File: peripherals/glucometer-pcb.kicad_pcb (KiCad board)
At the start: 2 copper layers, 244.2 x 145.5 mm, 126 parts, among them U1 ESP32_DevKit_V1_DOIT

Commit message: added 3D models
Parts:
- removed the 100nF1 at (35.7, 153.9)
- removed the 100nF1 at (72.2, 30.6)
- removed the 100nF1 at (170.3, 156.4)
- removed the 100nF1 at (234.8, 30.6)
- removed the 100nF1 at (181.4, 30.6)
- removed the 100nF1 at (123.0, 30.6)
- removed the 3V3_OUT1 at (88.9, 21.8)
- removed the 3V3_OUT1 at (198.1, 21.8)
- removed the 3V3_OUT1 at (161.5, 139.7)
- removed the 3V3_OUT1 at (251.5, 21.8)
- removed the 3V3_OUT1 at (139.7, 21.8)
- removed the 3V3_OUT1 at (26.9, 137.1)
- removed the BATTERY1 at (26.9, 151.3)
- removed the BATTERY1 at (237.3, 21.8)
- removed the BATTERY1 at (183.9, 21.8)
- removed the BATTERY1 at (125.5, 21.8)
- removed the BATTERY1 at (74.7, 21.8)
- removed the BATTERY1 at (161.5, 153.9)
- removed the BZ1 at (148.7, 32.9)
- removed the BZ1 at (172.6, 130.7)
- removed the BZ1 at (207.1, 32.9)
- removed the BZ1 at (260.5, 32.9)
- removed the BZ1 at (97.9, 32.9)
- removed the BZ1 at (38.0, 128.2)
- removed the D1 at (253.2, 145.1)
- removed the D1 at (83.5, 113.5)
- removed the D1 at (192.7, 113.5)
- removed the D1 at (246.1, 113.5)
- removed the D1 at (118.5, 142.5)
- removed the D1 at (134.3, 113.5)
- removed the GND1 at (238.1, 42.0)
- removed the GND1 at (126.4, 42.0)
- removed the GND1 at (47.1, 150.5)
- removed the GND1 at (75.6, 42.0)
- removed the GND1 at (181.7, 153.0)
- removed the GND1 at (184.8, 42.0)
- removed the INTERRUPT_GPIO1 at (161.5, 130.0)
- removed the INTERRUPT_GPIO1 at (149.4, 21.8)
- removed the INTERRUPT_GPIO1 at (98.6, 21.8)
- removed the INTERRUPT_GPIO1 at (261.2, 21.8)
- removed the INTERRUPT_GPIO1 at (26.9, 127.4)
- removed the INTERRUPT_GPIO1 at (207.8, 21.8)
- removed the R1 at (82.6, 35.7)
- removed the R1 at (133.4, 35.7)
- removed the R1 at (175.4, 146.0)
- removed the R1 at (191.8, 35.7)
- removed the R1 at (40.8, 143.5)
- removed the R1 at (245.1, 35.7)
- removed the R2 at (77.8, 35.7)
- removed the R2 at (187.1, 35.7)
- removed the R2 at (40.8, 148.2)
- removed the R2 at (128.6, 35.7)
- removed the R2 at (240.4, 35.7)
- removed the R2 at (175.4, 150.8)
- removed the REF** at (22.8, 154.8)
- removed the REF** at (71.3, 114.5)
- removed the REF** at (157.4, 157.3)
- removed the REF** at (261.6, 17.7)
- removed the REF** at (254.2, 157.3)
- removed the REF** at (122.1, 17.7)
- removed the REF** at (122.1, 114.5)
- removed the REF** at (207.8, 114.5)
- removed the REF** at (149.4, 114.5)
- removed the REF** at (149.8, 17.7)
- removed the REF** at (233.8, 17.7)
- removed the REF** at (261.2, 114.5)
- removed the REF** at (254.2, 130.0)
- removed the REF** at (98.6, 114.5)
- removed the REF** at (157.4, 129.6)
- removed the REF** at (119.6, 154.8)
- removed the REF** at (180.5, 17.7)
- removed the REF** at (99.0, 17.7)
- removed the REF** at (71.3, 17.7)
- removed the REF** at (180.5, 114.5)
- removed the REF** at (119.6, 127.5)
- removed the REF** at (22.8, 127.1)
- removed the REF** at (233.8, 114.5)
- removed the REF** at (208.2, 17.7)
- removed the SCL1 at (92.4, 42.0)
- removed the SCL1 at (47.1, 133.7)
- removed the SCL1 at (201.6, 42.0)
- removed the SCL1 at (181.7, 136.2)
- removed the SCL1 at (254.9, 42.0)
- removed the SCL1 at (143.2, 42.0)
- removed the SDA1 at (196.0, 42.0)
- removed the SDA1 at (137.6, 42.0)
- removed the SDA1 at (86.8, 42.0)
- removed the SDA1 at (47.1, 139.3)
- removed the SDA1 at (249.3, 42.0)
- removed the SDA1 at (181.7, 141.8)
- removed the SIGNAL_IN1 at (81.1, 21.8)
- removed the SIGNAL_IN1 at (161.5, 147.5)
- removed the SIGNAL_IN1 at (26.9, 144.9)
- removed the SIGNAL_IN1 at (131.9, 21.8)
- removed the SIGNAL_IN1 at (190.3, 21.8)
- removed the SIGNAL_IN1 at (243.7, 21.8)
- removed the U1 at (246.6, 86.0)
- removed the U1 at (134.8, 86.0)
- removed the U1 at (91.0, 142.1)
- removed the U1 at (193.2, 86.0)
- removed the U1 at (225.7, 144.6)
- removed the U1 at (84.0, 86.0)
- removed the VCC1 at (243.8, 42.0)
- removed the VCC1 at (190.5, 42.0)
- removed the VCC1 at (181.7, 147.3)
- removed the VCC1 at (81.3, 42.0)
- removed the VCC1 at (47.1, 144.8)
- removed the VCC1 at (132.1, 42.0)
- moved U1 0.06 mm to (36.0, 85.9)
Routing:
- net Net-(D1-Pad1): track 560.9 -> 80.1 mm
- net Net-(INTERRUPT_GPIO1-Pad1): track 376.7 -> 53.8 mm
- net Net-(3V3_OUT1-Pad1): track 342.0 -> 48.9 mm
- net Net-(SDA1-Pad1): track 318.6 -> 45.5 mm
- net Net-(100nF1-Pad2): track 313.1 -> 44.7 mm
- net Net-(BZ1-Pad1): track 270.9 -> 38.7 mm
- net Net-(SCL1-Pad1): track 249.0 -> 35.6 mm
- net Net-(BATTERY1-Pad1): track 232.0 -> 33.1 mm
- net Net-(D1-Pad2): track 223.4 -> 31.9 mm
- net Net-(100nF1-Pad1): track 88.0 -> 12.6 mm
- net Net-(BZ1-Pad2): track 55.2 -> 7.89 mm
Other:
- board size 244.2 x 145.5 mm -> 33.3 x 102.6 mm

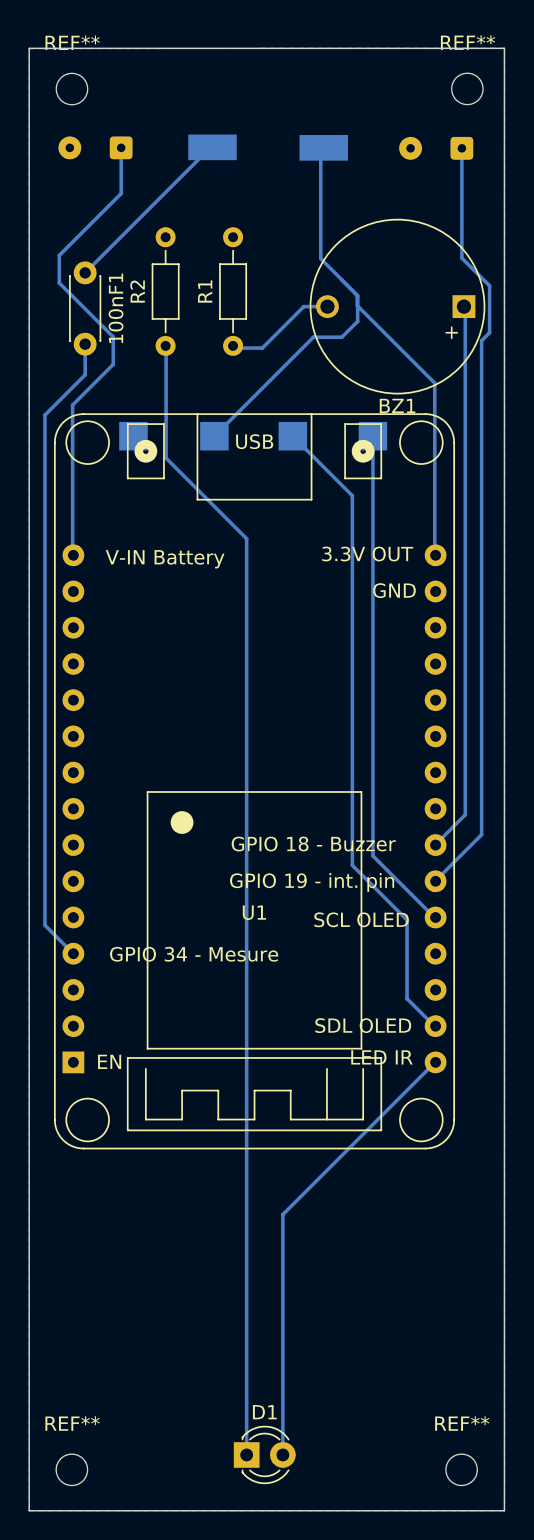
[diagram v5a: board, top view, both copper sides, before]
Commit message: updated pcb pads
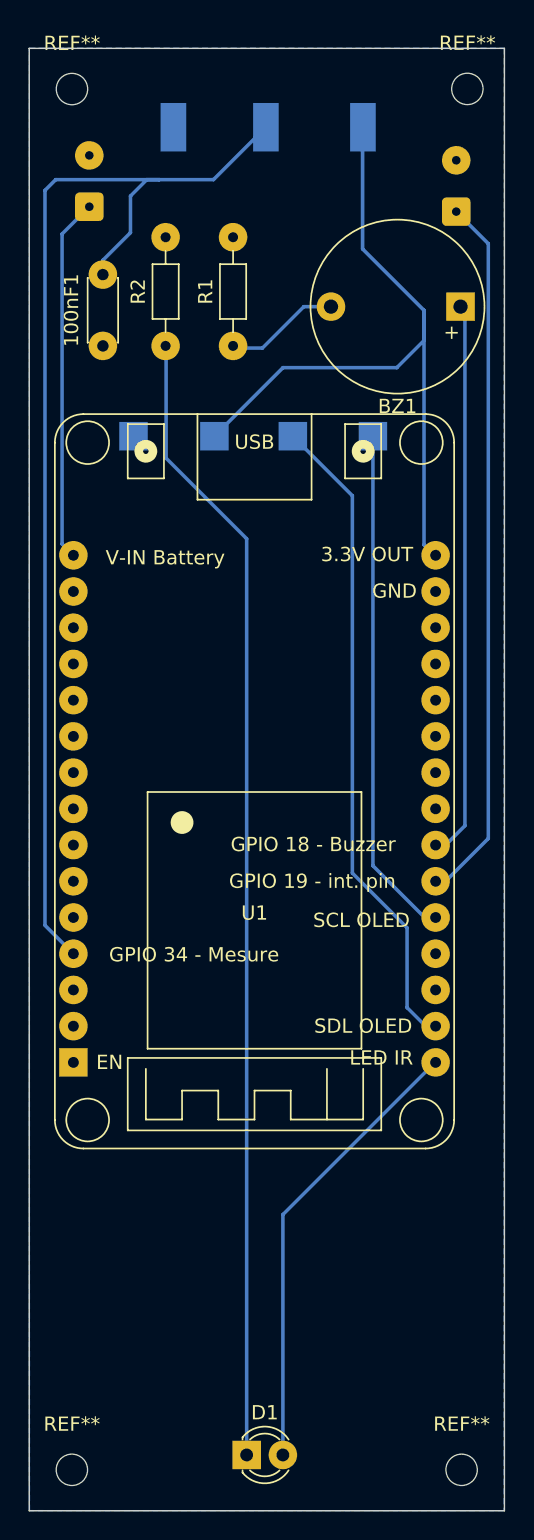
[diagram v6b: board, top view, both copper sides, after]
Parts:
- added GND1: TestPoint, TestPoint:TestPoint_Keystone_5015_Micro-Minature, B.Cu at (30.3, 20.4)
- moved 100nF1 5.27 mm to (25.4, 35.7), turned to 90 degrees
- moved BATTERY1 4.69 mm to (24.4, 25.9), turned to 90 degrees
- moved INTERRUPT_GPIO1 4.46 mm to (50.2, 26.3), turned to 90 degrees
- moved SIGNAL_IN1 4.00 mm to (36.8, 20.4), turned to -90 degrees
- moved 3V3_OUT1 3.11 mm to (43.6, 20.4), turned to -90 degrees
- renumbered GND1 to GND2
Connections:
- 100nF1 pad 1: Net-(100nF1-Pad1) -> GND
- SIGNAL_IN1 pad 1: Net-(100nF1-Pad1) -> Net-(100nF1-Pad2)
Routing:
- net Net-(100nF1-Pad2): track 44.7 -> 80.5 mm
- net Net-(100nF1-Pad1): track 12.6 -> 0.00 mm
- net Net-(BATTERY1-Pad1): track 33.1 -> 25.6 mm
- net Net-(INTERRUPT_GPIO1-Pad1): track 53.8 -> 49.8 mm
- net Net-(3V3_OUT1-Pad1): track 48.9 -> 51.7 mm
- net Net-(BZ1-Pad1): track 38.7 -> 39.4 mm

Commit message: added pdfs
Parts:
- added 100nF1: CAP, Capacitor_THT:C_Disc_D4.3mm_W1.9mm_P5.00mm, F.Cu at (111.1, 37.0)
- added 100nF1: CAP, Capacitor_THT:C_Disc_D4.3mm_W1.9mm_P5.00mm, F.Cu at (47.1, 167.8)
- added 100nF1: CAP, Capacitor_THT:C_Disc_D4.3mm_W1.9mm_P5.00mm, F.Cu at (181.7, 165.3)
- added 100nF1: CAP, Capacitor_THT:C_Disc_D4.3mm_W1.9mm_P5.00mm, F.Cu at (197.9, 37.0)
- added 100nF1: CAP, Capacitor_THT:C_Disc_D4.3mm_W1.9mm_P5.00mm, F.Cu at (154.5, 36.2)
- added 100nF1: CAP, Capacitor_THT:C_Disc_D4.3mm_W1.9mm_P5.00mm, F.Cu at (246.2, 37.0)
- added 100nF1: CAP, Capacitor_THT:C_Disc_D4.3mm_W1.9mm_P5.00mm, F.Cu at (67.7, 36.2)
- added 3V3_OUT1: TestPoint, TestPoint:TestPoint_Keystone_5015_Micro-Minature, B.Cu at (31.8, 149.6)
- added 3V3_OUT1: TestPoint, TestPoint:TestPoint_Keystone_5015_Micro-Minature, B.Cu at (264.4, 21.6)
- added 3V3_OUT1: TestPoint, TestPoint:TestPoint_Keystone_5015_Micro-Minature, B.Cu at (216.2, 21.6)
- added 3V3_OUT1: TestPoint, TestPoint:TestPoint_Keystone_5015_Micro-Minature, B.Cu at (172.8, 20.9)
- added 3V3_OUT1: TestPoint, TestPoint:TestPoint_Keystone_5015_Micro-Minature, B.Cu at (86.0, 20.9)
- added 3V3_OUT1: TestPoint, TestPoint:TestPoint_Keystone_5015_Micro-Minature, B.Cu at (166.4, 147.1)
- added 3V3_OUT1: TestPoint, TestPoint:TestPoint_Keystone_5015_Micro-Minature, B.Cu at (129.3, 21.6)
- added BATTERY1: Battery_Cell, Connector_Wire:SolderWire-0.1sqmm_1x02_P3.6mm_D0.4mm_OD1mm, B.Cu at (197.0, 27.2)
- added BATTERY1: Battery_Cell, Connector_Wire:SolderWire-0.1sqmm_1x02_P3.6mm_D0.4mm_OD1mm, B.Cu at (110.1, 27.2)
- added BATTERY1: Battery_Cell, Connector_Wire:SolderWire-0.1sqmm_1x02_P3.6mm_D0.4mm_OD1mm, B.Cu at (172.0, 166.3)
- added BATTERY1: Battery_Cell, Connector_Wire:SolderWire-0.1sqmm_1x02_P3.6mm_D0.4mm_OD1mm, B.Cu at (66.8, 26.5)
- added BATTERY1: Battery_Cell, Connector_Wire:SolderWire-0.1sqmm_1x02_P3.6mm_D0.4mm_OD1mm, B.Cu at (153.6, 26.5)
- added BATTERY1: Battery_Cell, Connector_Wire:SolderWire-0.1sqmm_1x02_P3.6mm_D0.4mm_OD1mm, B.Cu at (245.2, 27.2)
- added BATTERY1: Battery_Cell, Connector_Wire:SolderWire-0.1sqmm_1x02_P3.6mm_D0.4mm_OD1mm, B.Cu at (37.4, 168.8)
- added BZ1: Buzzer, Buzzer_Beeper:MagneticBuzzer_ProSignal_ABI-009-RC, F.Cu at (92.2, 33.5)
- added BZ1: Buzzer, Buzzer_Beeper:MagneticBuzzer_ProSignal_ABI-009-RC, F.Cu at (44.4, 143.4)
- added BZ1: Buzzer, Buzzer_Beeper:MagneticBuzzer_ProSignal_ABI-009-RC, F.Cu at (222.4, 34.2)
- added BZ1: Buzzer, Buzzer_Beeper:MagneticBuzzer_ProSignal_ABI-009-RC, F.Cu at (179.0, 33.5)
- added BZ1: Buzzer, Buzzer_Beeper:MagneticBuzzer_ProSignal_ABI-009-RC, F.Cu at (135.6, 34.2)
- added BZ1: Buzzer, Buzzer_Beeper:MagneticBuzzer_ProSignal_ABI-009-RC, F.Cu at (270.6, 34.2)
- added BZ1: Buzzer, Buzzer_Beeper:MagneticBuzzer_ProSignal_ABI-009-RC, F.Cu at (179.0, 140.8)
- added D1: EMITTER, LED_THT:LED_D3.0mm_Clear, F.Cu at (164.6, 114.0)
- added D1: EMITTER, LED_THT:LED_D3.0mm_Clear, F.Cu at (259.5, 155.2)
- added D1: EMITTER, LED_THT:LED_D3.0mm_Clear, F.Cu at (77.8, 114.0)
- added D1: EMITTER, LED_THT:LED_D3.0mm_Clear, F.Cu at (121.2, 114.7)
- added D1: EMITTER, LED_THT:LED_D3.0mm_Clear, F.Cu at (208.0, 114.7)
- added D1: EMITTER, LED_THT:LED_D3.0mm_Clear, F.Cu at (256.3, 114.7)
- added D1: EMITTER, LED_THT:LED_D3.0mm_Clear, F.Cu at (124.9, 157.8)
- added GND1: TestPoint, TestPoint:TestPoint_Keystone_5015_Micro-Minature, B.Cu at (251.1, 21.6)
- added GND1: TestPoint, TestPoint:TestPoint_Keystone_5015_Micro-Minature, B.Cu at (116.0, 21.6)
- added GND1: TestPoint, TestPoint:TestPoint_Keystone_5015_Micro-Minature, B.Cu at (166.4, 160.4)
- added GND1: TestPoint, TestPoint:TestPoint_Keystone_5015_Micro-Minature, B.Cu at (72.7, 20.9)
- added GND1: TestPoint, TestPoint:TestPoint_Keystone_5015_Micro-Minature, B.Cu at (159.5, 20.9)
- added GND1: TestPoint, TestPoint:TestPoint_Keystone_5015_Micro-Minature, B.Cu at (202.9, 21.6)
- added GND1: TestPoint, TestPoint:TestPoint_Keystone_5015_Micro-Minature, B.Cu at (31.8, 162.9)
- added GND2: TestPoint, TestPoint:TestPoint_Pad_2.0x2.0mm, B.Cu at (113.2, 43.3)
- added GND2: TestPoint, TestPoint:TestPoint_Pad_2.0x2.0mm, B.Cu at (200.1, 43.3)
- added GND2: TestPoint, TestPoint:TestPoint_Pad_2.0x2.0mm, B.Cu at (69.9, 42.6)
- added GND2: TestPoint, TestPoint:TestPoint_Pad_2.0x2.0mm, B.Cu at (188.1, 163.2)
- added GND2: TestPoint, TestPoint:TestPoint_Pad_2.0x2.0mm, B.Cu at (248.3, 43.3)
- added GND2: TestPoint, TestPoint:TestPoint_Pad_2.0x2.0mm, B.Cu at (53.5, 165.7)
- added GND2: TestPoint, TestPoint:TestPoint_Pad_2.0x2.0mm, B.Cu at (156.7, 42.6)
- added INTERRUPT_GPIO1: SW_Push, Connector_Wire:SolderWire-0.1sqmm_1x02_P3.6mm_D0.4mm_OD1mm, B.Cu at (92.5, 26.8)
- added INTERRUPT_GPIO1: SW_Push, Connector_Wire:SolderWire-0.1sqmm_1x02_P3.6mm_D0.4mm_OD1mm, B.Cu at (172.3, 140.5)
- added INTERRUPT_GPIO1: SW_Push, Connector_Wire:SolderWire-0.1sqmm_1x02_P3.6mm_D0.4mm_OD1mm, B.Cu at (271.0, 27.6)
- added INTERRUPT_GPIO1: SW_Push, Connector_Wire:SolderWire-0.1sqmm_1x02_P3.6mm_D0.4mm_OD1mm, B.Cu at (179.3, 26.8)
- added INTERRUPT_GPIO1: SW_Push, Connector_Wire:SolderWire-0.1sqmm_1x02_P3.6mm_D0.4mm_OD1mm, B.Cu at (135.9, 27.5)
- added INTERRUPT_GPIO1: SW_Push, Connector_Wire:SolderWire-0.1sqmm_1x02_P3.6mm_D0.4mm_OD1mm, B.Cu at (37.7, 143.1)
- added INTERRUPT_GPIO1: SW_Push, Connector_Wire:SolderWire-0.1sqmm_1x02_P3.6mm_D0.4mm_OD1mm, B.Cu at (222.7, 27.5)
- added R1: 120, Resistor_THT:R_Axial_DIN0204_L3.6mm_D1.6mm_P7.62mm_Horizontal, F.Cu at (120.2, 37.0)
- added R1: 120, Resistor_THT:R_Axial_DIN0204_L3.6mm_D1.6mm_P7.62mm_Horizontal, F.Cu at (76.9, 36.2)
- added R1: 120, Resistor_THT:R_Axial_DIN0204_L3.6mm_D1.6mm_P7.62mm_Horizontal, F.Cu at (207.0, 37.0)
- added R1: 120, Resistor_THT:R_Axial_DIN0204_L3.6mm_D1.6mm_P7.62mm_Horizontal, F.Cu at (163.7, 36.2)
- added R1: 120, Resistor_THT:R_Axial_DIN0204_L3.6mm_D1.6mm_P7.62mm_Horizontal, F.Cu at (255.3, 37.0)
- added R1: 120, Resistor_THT:R_Axial_DIN0204_L3.6mm_D1.6mm_P7.62mm_Horizontal, F.Cu at (181.7, 156.2)
- added R1: 120, Resistor_THT:R_Axial_DIN0204_L3.6mm_D1.6mm_P7.62mm_Horizontal, F.Cu at (47.1, 158.7)
- added R2: 120, Resistor_THT:R_Axial_DIN0204_L3.6mm_D1.6mm_P7.62mm_Horizontal, F.Cu at (47.1, 163.4)
- added R2: 120, Resistor_THT:R_Axial_DIN0204_L3.6mm_D1.6mm_P7.62mm_Horizontal, F.Cu at (250.6, 37.0)
- added R2: 120, Resistor_THT:R_Axial_DIN0204_L3.6mm_D1.6mm_P7.62mm_Horizontal, F.Cu at (202.3, 37.0)
- added R2: 120, Resistor_THT:R_Axial_DIN0204_L3.6mm_D1.6mm_P7.62mm_Horizontal, F.Cu at (115.5, 37.0)
- added R2: 120, Resistor_THT:R_Axial_DIN0204_L3.6mm_D1.6mm_P7.62mm_Horizontal, F.Cu at (72.1, 36.2)
- added R2: 120, Resistor_THT:R_Axial_DIN0204_L3.6mm_D1.6mm_P7.62mm_Horizontal, F.Cu at (158.9, 36.2)
- added R2: 120, Resistor_THT:R_Axial_DIN0204_L3.6mm_D1.6mm_P7.62mm_Horizontal, F.Cu at (181.7, 160.9)
- added REF**: MountingHole_2.2mm_M2, MountingHole:MountingHole_2.2mm_M2, F.Cu at (195.8, 19.0)
- added REF**: MountingHole_2.2mm_M2, MountingHole:MountingHole_2.2mm_M2, F.Cu at (136.7, 18.9)
- added REF**: MountingHole_2.2mm_M2, MountingHole:MountingHole_2.2mm_M2, F.Cu at (260.6, 140.1)
- added REF**: MountingHole_2.2mm_M2, MountingHole:MountingHole_2.2mm_M2, F.Cu at (125.9, 142.7)
- added REF**: MountingHole_2.2mm_M2, MountingHole:MountingHole_2.2mm_M2, F.Cu at (29.1, 170.0)
- added REF**: MountingHole_2.2mm_M2, MountingHole:MountingHole_2.2mm_M2, F.Cu at (271.7, 18.9)
- added REF**: MountingHole_2.2mm_M2, MountingHole:MountingHole_2.2mm_M2, F.Cu at (136.3, 115.8)
- added REF**: MountingHole_2.2mm_M2, MountingHole:MountingHole_2.2mm_M2, F.Cu at (65.6, 18.2)
- added REF**: MountingHole_2.2mm_M2, MountingHole:MountingHole_2.2mm_M2, F.Cu at (244.0, 115.8)
- added REF**: MountingHole_2.2mm_M2, MountingHole:MountingHole_2.2mm_M2, F.Cu at (163.7, 167.5)
- added REF**: MountingHole_2.2mm_M2, MountingHole:MountingHole_2.2mm_M2, F.Cu at (223.1, 115.8)
- added REF**: MountingHole_2.2mm_M2, MountingHole:MountingHole_2.2mm_M2, F.Cu at (125.9, 170.0)
- added REF**: MountingHole_2.2mm_M2, MountingHole:MountingHole_2.2mm_M2, F.Cu at (65.5, 115.0)
- added REF**: MountingHole_2.2mm_M2, MountingHole:MountingHole_2.2mm_M2, F.Cu at (108.9, 115.8)
- added REF**: MountingHole_2.2mm_M2, MountingHole:MountingHole_2.2mm_M2, F.Cu at (223.5, 18.9)
- added REF**: MountingHole_2.2mm_M2, MountingHole:MountingHole_2.2mm_M2, F.Cu at (29.1, 142.3)
- added REF**: MountingHole_2.2mm_M2, MountingHole:MountingHole_2.2mm_M2, F.Cu at (163.7, 139.7)
- added REF**: MountingHole_2.2mm_M2, MountingHole:MountingHole_2.2mm_M2, F.Cu at (93.3, 18.2)
- added REF**: MountingHole_2.2mm_M2, MountingHole:MountingHole_2.2mm_M2, F.Cu at (179.7, 115.0)
- added REF**: MountingHole_2.2mm_M2, MountingHole:MountingHole_2.2mm_M2, F.Cu at (92.9, 115.0)
- added REF**: MountingHole_2.2mm_M2, MountingHole:MountingHole_2.2mm_M2, F.Cu at (271.3, 115.8)
- added REF**: MountingHole_2.2mm_M2, MountingHole:MountingHole_2.2mm_M2, F.Cu at (244.0, 19.0)
- added REF**: MountingHole_2.2mm_M2, MountingHole:MountingHole_2.2mm_M2, F.Cu at (108.9, 19.0)
- added REF**: MountingHole_2.2mm_M2, MountingHole:MountingHole_2.2mm_M2, F.Cu at (260.6, 167.5)
- added REF**: MountingHole_2.2mm_M2, MountingHole:MountingHole_2.2mm_M2, F.Cu at (152.4, 115.0)
- added REF**: MountingHole_2.2mm_M2, MountingHole:MountingHole_2.2mm_M2, F.Cu at (195.7, 115.8)
- added REF**: MountingHole_2.2mm_M2, MountingHole:MountingHole_2.2mm_M2, F.Cu at (152.4, 18.2)
- added REF**: MountingHole_2.2mm_M2, MountingHole:MountingHole_2.2mm_M2, F.Cu at (180.1, 18.2)
- added SCL1: TestPoint, TestPoint:TestPoint_Pad_2.0x2.0mm, B.Cu at (216.9, 43.3)
- added SCL1: TestPoint, TestPoint:TestPoint_Pad_2.0x2.0mm, B.Cu at (173.5, 42.6)
- added SCL1: TestPoint, TestPoint:TestPoint_Pad_2.0x2.0mm, B.Cu at (53.5, 148.9)
- added SCL1: TestPoint, TestPoint:TestPoint_Pad_2.0x2.0mm, B.Cu at (130.0, 43.3)
- added SCL1: TestPoint, TestPoint:TestPoint_Pad_2.0x2.0mm, B.Cu at (188.1, 146.4)
- added SCL1: TestPoint, TestPoint:TestPoint_Pad_2.0x2.0mm, B.Cu at (86.7, 42.6)
- added SCL1: TestPoint, TestPoint:TestPoint_Pad_2.0x2.0mm, B.Cu at (265.1, 43.3)
- added SDA1: TestPoint, TestPoint:TestPoint_Pad_2.0x2.0mm, B.Cu at (259.5, 43.3)
- added SDA1: TestPoint, TestPoint:TestPoint_Pad_2.0x2.0mm, B.Cu at (211.2, 43.3)
- added SDA1: TestPoint, TestPoint:TestPoint_Pad_2.0x2.0mm, B.Cu at (167.9, 42.6)
- added SDA1: TestPoint, TestPoint:TestPoint_Pad_2.0x2.0mm, B.Cu at (188.1, 152.0)
- added SDA1: TestPoint, TestPoint:TestPoint_Pad_2.0x2.0mm, B.Cu at (53.5, 154.5)
- added SDA1: TestPoint, TestPoint:TestPoint_Pad_2.0x2.0mm, B.Cu at (81.0, 42.6)
- added SDA1: TestPoint, TestPoint:TestPoint_Pad_2.0x2.0mm, B.Cu at (124.4, 43.3)
- added SIGNAL_IN1: TestPoint, TestPoint:TestPoint_Keystone_5015_Micro-Minature, B.Cu at (166.4, 153.9)
- added SIGNAL_IN1: TestPoint, TestPoint:TestPoint_Keystone_5015_Micro-Minature, B.Cu at (209.3, 21.6)
- added SIGNAL_IN1: TestPoint, TestPoint:TestPoint_Keystone_5015_Micro-Minature, B.Cu at (166.0, 20.9)
- added SIGNAL_IN1: TestPoint, TestPoint:TestPoint_Keystone_5015_Micro-Minature, B.Cu at (122.5, 21.6)
- added SIGNAL_IN1: TestPoint, TestPoint:TestPoint_Keystone_5015_Micro-Minature, B.Cu at (79.2, 20.9)
- added SIGNAL_IN1: TestPoint, TestPoint:TestPoint_Keystone_5015_Micro-Minature, B.Cu at (257.6, 21.6)
- added SIGNAL_IN1: TestPoint, TestPoint:TestPoint_Keystone_5015_Micro-Minature, B.Cu at (31.8, 156.4)
- added U1: ESP32_DevKit_V1_DOIT, esp32_devkit_v1_doit:esp32_devkit_v1_doit, F.Cu at (165.2, 86.5)
- added U1: ESP32_DevKit_V1_DOIT, esp32_devkit_v1_doit:esp32_devkit_v1_doit, F.Cu at (256.8, 87.2)
- added U1: ESP32_DevKit_V1_DOIT, esp32_devkit_v1_doit:esp32_devkit_v1_doit, F.Cu at (97.4, 157.2)
- added U1: ESP32_DevKit_V1_DOIT, esp32_devkit_v1_doit:esp32_devkit_v1_doit, F.Cu at (208.6, 87.2)
- added U1: ESP32_DevKit_V1_DOIT, esp32_devkit_v1_doit:esp32_devkit_v1_doit, F.Cu at (232.0, 154.7)
- added U1: ESP32_DevKit_V1_DOIT, esp32_devkit_v1_doit:esp32_devkit_v1_doit, F.Cu at (121.7, 87.2)
- added U1: ESP32_DevKit_V1_DOIT, esp32_devkit_v1_doit:esp32_devkit_v1_doit, F.Cu at (78.4, 86.5)
- added VCC1: TestPoint, TestPoint:TestPoint_Pad_2.0x2.0mm, B.Cu at (188.1, 157.5)
- added VCC1: TestPoint, TestPoint:TestPoint_Pad_2.0x2.0mm, B.Cu at (53.5, 160.0)
- added VCC1: TestPoint, TestPoint:TestPoint_Pad_2.0x2.0mm, B.Cu at (118.9, 43.3)
- added VCC1: TestPoint, TestPoint:TestPoint_Pad_2.0x2.0mm, B.Cu at (254.0, 43.3)
- added VCC1: TestPoint, TestPoint:TestPoint_Pad_2.0x2.0mm, B.Cu at (205.7, 43.3)
- added VCC1: TestPoint, TestPoint:TestPoint_Pad_2.0x2.0mm, B.Cu at (75.5, 42.6)
- added VCC1: TestPoint, TestPoint:TestPoint_Pad_2.0x2.0mm, B.Cu at (162.4, 42.6)
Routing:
- net Net-(100nF1-Pad2): track 80.5 -> 643.9 mm
- net Net-(D1-Pad1): track 80.1 -> 641.0 mm
- net Net-(INTERRUPT_GPIO1-Pad1): track 49.8 -> 398.6 mm
- net Net-(3V3_OUT1-Pad1): track 51.7 -> 391.8 mm
- net Net-(SDA1-Pad1): track 45.9 -> 367.4 mm
- net Net-(BZ1-Pad1): track 39.4 -> 315.2 mm
- net Net-(SCL1-Pad1): track 36.0 -> 288.2 mm
- net Net-(D1-Pad2): track 31.9 -> 255.4 mm
- net Net-(BATTERY1-Pad1): track 25.6 -> 204.5 mm
- net Net-(BZ1-Pad2): track 8.13 -> 71.8 mm
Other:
- board size 33.3 x 102.6 mm -> 254.1 x 158.2 mm

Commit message: updated PCBs
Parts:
- removed the 100nF1 at (111.1, 37.0)
- removed the 100nF1 at (47.1, 167.8)
- removed the 100nF1 at (181.7, 165.3)
- removed the 100nF1 at (197.9, 37.0)
- removed the 100nF1 at (154.5, 36.2)
- removed the 100nF1 at (246.2, 37.0)
- removed the 100nF1 at (67.7, 36.2)
- removed the 3V3_OUT1 at (31.8, 149.6)
- removed the 3V3_OUT1 at (264.4, 21.6)
- removed the 3V3_OUT1 at (216.2, 21.6)
- removed the 3V3_OUT1 at (172.8, 20.9)
- removed the 3V3_OUT1 at (86.0, 20.9)
- removed the 3V3_OUT1 at (166.4, 147.1)
- removed the 3V3_OUT1 at (129.3, 21.6)
- removed the BATTERY1 at (197.0, 27.2)
- removed the BATTERY1 at (110.1, 27.2)
- removed the BATTERY1 at (172.0, 166.3)
- removed the BATTERY1 at (66.8, 26.5)
- removed the BATTERY1 at (153.6, 26.5)
- removed the BATTERY1 at (245.2, 27.2)
- removed the BATTERY1 at (37.4, 168.8)
- removed the BZ1 at (92.2, 33.5)
- removed the BZ1 at (44.4, 143.4)
- removed the BZ1 at (222.4, 34.2)
- removed the BZ1 at (179.0, 33.5)
- removed the BZ1 at (135.6, 34.2)
- removed the BZ1 at (270.6, 34.2)
- removed the BZ1 at (179.0, 140.8)
- removed the D1 at (164.6, 114.0)
- removed the D1 at (259.5, 155.2)
- removed the D1 at (77.8, 114.0)
- removed the D1 at (121.2, 114.7)
- removed the D1 at (208.0, 114.7)
- removed the D1 at (256.3, 114.7)
- removed the D1 at (124.9, 157.8)
- removed the GND1 at (251.1, 21.6)
- removed the GND1 at (116.0, 21.6)
- removed the GND1 at (166.4, 160.4)
- removed the GND1 at (72.7, 20.9)
- removed the GND1 at (159.5, 20.9)
- removed the GND1 at (202.9, 21.6)
- removed the GND1 at (31.8, 162.9)
- removed the GND2 at (113.2, 43.3)
- removed the GND2 at (200.1, 43.3)
- removed the GND2 at (69.9, 42.6)
- removed the GND2 at (188.1, 163.2)
- removed the GND2 at (248.3, 43.3)
- removed the GND2 at (53.5, 165.7)
- removed the GND2 at (156.7, 42.6)
- removed the INTERRUPT_GPIO1 at (92.5, 26.8)
- removed the INTERRUPT_GPIO1 at (172.3, 140.5)
- removed the INTERRUPT_GPIO1 at (271.0, 27.6)
- removed the INTERRUPT_GPIO1 at (179.3, 26.8)
- removed the INTERRUPT_GPIO1 at (135.9, 27.5)
- removed the INTERRUPT_GPIO1 at (37.7, 143.1)
- removed the INTERRUPT_GPIO1 at (222.7, 27.5)
- removed the R1 at (120.2, 37.0)
- removed the R1 at (76.9, 36.2)
- removed the R1 at (207.0, 37.0)
- removed the R1 at (163.7, 36.2)
- removed the R1 at (255.3, 37.0)
- removed the R1 at (181.7, 156.2)
- removed the R1 at (47.1, 158.7)
- removed the R2 at (47.1, 163.4)
- removed the R2 at (250.6, 37.0)
- removed the R2 at (202.3, 37.0)
- removed the R2 at (115.5, 37.0)
- removed the R2 at (72.1, 36.2)
- removed the R2 at (158.9, 36.2)
- removed the R2 at (181.7, 160.9)
- removed the REF** at (195.8, 19.0)
- removed the REF** at (136.7, 18.9)
- removed the REF** at (260.6, 140.1)
- removed the REF** at (125.9, 142.7)
- removed the REF** at (29.1, 170.0)
- removed the REF** at (271.7, 18.9)
- removed the REF** at (136.3, 115.8)
- removed the REF** at (65.6, 18.2)
- removed the REF** at (244.0, 115.8)
- removed the REF** at (163.7, 167.5)
- removed the REF** at (223.1, 115.8)
- removed the REF** at (125.9, 170.0)
- removed the REF** at (65.5, 115.0)
- removed the REF** at (108.9, 115.8)
- removed the REF** at (223.5, 18.9)
- removed the REF** at (29.1, 142.3)
- removed the REF** at (163.7, 139.7)
- removed the REF** at (93.3, 18.2)
- removed the REF** at (179.7, 115.0)
- removed the REF** at (92.9, 115.0)
- removed the REF** at (271.3, 115.8)
- removed the REF** at (244.0, 19.0)
- removed the REF** at (108.9, 19.0)
- removed the REF** at (260.6, 167.5)
- removed the REF** at (152.4, 115.0)
- removed the REF** at (195.7, 115.8)
- removed the REF** at (152.4, 18.2)
- removed the REF** at (180.1, 18.2)
- removed the SCL1 at (216.9, 43.3)
- removed the SCL1 at (173.5, 42.6)
- removed the SCL1 at (53.5, 148.9)
- removed the SCL1 at (130.0, 43.3)
- removed the SCL1 at (188.1, 146.4)
- removed the SCL1 at (86.7, 42.6)
- removed the SCL1 at (265.1, 43.3)
- removed the SDA1 at (259.5, 43.3)
- removed the SDA1 at (211.2, 43.3)
- removed the SDA1 at (167.9, 42.6)
- removed the SDA1 at (188.1, 152.0)
- removed the SDA1 at (53.5, 154.5)
- removed the SDA1 at (81.0, 42.6)
- removed the SDA1 at (124.4, 43.3)
- removed the SIGNAL_IN1 at (166.4, 153.9)
- removed the SIGNAL_IN1 at (209.3, 21.6)
- removed the SIGNAL_IN1 at (166.0, 20.9)
- removed the SIGNAL_IN1 at (122.5, 21.6)
- removed the SIGNAL_IN1 at (79.2, 20.9)
- removed the SIGNAL_IN1 at (257.6, 21.6)
- removed the SIGNAL_IN1 at (31.8, 156.4)
- removed the U1 at (165.2, 86.5)
- removed the U1 at (256.8, 87.2)
- removed the U1 at (97.4, 157.2)
- removed the U1 at (208.6, 87.2)
- removed the U1 at (232.0, 154.7)
- removed the U1 at (121.7, 87.2)
- removed the U1 at (78.4, 86.5)
- removed the VCC1 at (188.1, 157.5)
- removed the VCC1 at (53.5, 160.0)
- removed the VCC1 at (118.9, 43.3)
- removed the VCC1 at (254.0, 43.3)
- removed the VCC1 at (205.7, 43.3)
- removed the VCC1 at (75.5, 42.6)
- removed the VCC1 at (162.4, 42.6)
- added 100nF1: CAP, Capacitor_THT:C_Disc_D4.3mm_W1.9mm_P5.00mm, F.Cu at (171.9, 153.1)
- added 100nF1: CAP, Capacitor_THT:C_Disc_D4.3mm_W1.9mm_P5.00mm, F.Cu at (216.9, 25.0)
- added 100nF1: CAP, Capacitor_THT:C_Disc_D4.3mm_W1.9mm_P5.00mm, F.Cu at (84.7, 25.0)
- added 100nF1: CAP, Capacitor_THT:C_Disc_D4.3mm_W1.9mm_P5.00mm, F.Cu at (262.5, 25.0)
- added 100nF1: CAP, Capacitor_THT:C_Disc_D4.3mm_W1.9mm_P5.00mm, F.Cu at (30.5, 153.8)
- added 100nF1: CAP, Capacitor_THT:C_Disc_D4.3mm_W1.9mm_P5.00mm, F.Cu at (173.6, 25.0)
- added 100nF1: CAP, Capacitor_THT:C_Disc_D4.3mm_W1.9mm_P5.00mm, F.Cu at (128.0, 25.0)
- added 3V3_OUT1: TestPoint, TestPoint:TestPoint_Keystone_5015_Micro-Minature, B.Cu at (267.0, 17.8)
- added 3V3_OUT1: TestPoint, TestPoint:TestPoint_Keystone_5015_Micro-Minature, B.Cu at (178.1, 17.8)
- added 3V3_OUT1: TestPoint, TestPoint:TestPoint_Keystone_5015_Micro-Minature, B.Cu at (89.2, 17.8)
- added 3V3_OUT1: TestPoint, TestPoint:TestPoint_Keystone_5015_Micro-Minature, B.Cu at (164.7, 148.6)
- added 3V3_OUT1: TestPoint, TestPoint:TestPoint_Keystone_5015_Micro-Minature, B.Cu at (23.3, 149.3)
- added 3V3_OUT1: TestPoint, TestPoint:TestPoint_Keystone_5015_Micro-Minature, B.Cu at (221.4, 17.8)
- added 3V3_OUT1: TestPoint, TestPoint:TestPoint_Keystone_5015_Micro-Minature, B.Cu at (132.5, 17.8)
- added BATTERY1: Battery_Cell, Connector_Wire:SolderWire-0.1sqmm_1x02_P3.6mm_D0.4mm_OD1mm, B.Cu at (30.5, 166.9)
- added BATTERY1: Battery_Cell, Connector_Wire:SolderWire-0.1sqmm_1x02_P3.6mm_D0.4mm_OD1mm, B.Cu at (203.8, 25.0)
- added BATTERY1: Battery_Cell, Connector_Wire:SolderWire-0.1sqmm_1x02_P3.6mm_D0.4mm_OD1mm, B.Cu at (71.5, 25.0)
- added BATTERY1: Battery_Cell, Connector_Wire:SolderWire-0.1sqmm_1x02_P3.6mm_D0.4mm_OD1mm, B.Cu at (160.4, 25.0)
- added BATTERY1: Battery_Cell, Connector_Wire:SolderWire-0.1sqmm_1x02_P3.6mm_D0.4mm_OD1mm, B.Cu at (171.9, 166.3)
- added BATTERY1: Battery_Cell, Connector_Wire:SolderWire-0.1sqmm_1x02_P3.6mm_D0.4mm_OD1mm, B.Cu at (249.3, 25.0)
- added BATTERY1: Battery_Cell, Connector_Wire:SolderWire-0.1sqmm_1x02_P3.6mm_D0.4mm_OD1mm, B.Cu at (114.9, 25.0)
- added BZ1: Buzzer, Buzzer_Beeper:MagneticBuzzer_ProSignal_ABI-009-RC, F.Cu at (32.5, 142.2)
- added BZ1: Buzzer, Buzzer_Beeper:MagneticBuzzer_ProSignal_ABI-009-RC, F.Cu at (96.3, 27.0)
- added BZ1: Buzzer, Buzzer_Beeper:MagneticBuzzer_ProSignal_ABI-009-RC, F.Cu at (173.9, 141.5)
- added BZ1: Buzzer, Buzzer_Beeper:MagneticBuzzer_ProSignal_ABI-009-RC, F.Cu at (228.5, 27.0)
- added BZ1: Buzzer, Buzzer_Beeper:MagneticBuzzer_ProSignal_ABI-009-RC, F.Cu at (185.2, 27.0)
- added BZ1: Buzzer, Buzzer_Beeper:MagneticBuzzer_ProSignal_ABI-009-RC, F.Cu at (274.1, 27.0)
- added BZ1: Buzzer, Buzzer_Beeper:MagneticBuzzer_ProSignal_ABI-009-RC, F.Cu at (139.6, 27.0)
- added D1: EMITTER, LED_THT:LED_D3.0mm_Clear, F.Cu at (124.4, 113.5)
- added D1: EMITTER, LED_THT:LED_D3.0mm_Clear, F.Cu at (260.3, 156.8)
- added D1: EMITTER, LED_THT:LED_D3.0mm_Clear, F.Cu at (81.0, 113.5)
- added D1: EMITTER, LED_THT:LED_D3.0mm_Clear, F.Cu at (119.0, 157.5)
- added D1: EMITTER, LED_THT:LED_D3.0mm_Clear, F.Cu at (258.8, 113.5)
- added D1: EMITTER, LED_THT:LED_D3.0mm_Clear, F.Cu at (169.9, 113.5)
- added D1: EMITTER, LED_THT:LED_D3.0mm_Clear, F.Cu at (213.3, 113.5)
- added GND1: TestPoint, TestPoint:TestPoint_Keystone_5015_Micro-Minature, B.Cu at (253.8, 17.8)
- added GND1: TestPoint, TestPoint:TestPoint_Keystone_5015_Micro-Minature, B.Cu at (76.0, 17.8)
- added GND1: TestPoint, TestPoint:TestPoint_Keystone_5015_Micro-Minature, B.Cu at (208.3, 17.8)
- added GND1: TestPoint, TestPoint:TestPoint_Keystone_5015_Micro-Minature, B.Cu at (164.9, 17.8)
- added GND1: TestPoint, TestPoint:TestPoint_Keystone_5015_Micro-Minature, B.Cu at (119.4, 17.8)
- added GND1: TestPoint, TestPoint:TestPoint_Keystone_5015_Micro-Minature, B.Cu at (164.7, 161.8)
- added GND1: TestPoint, TestPoint:TestPoint_Keystone_5015_Micro-Minature, B.Cu at (23.3, 162.5)
- added GND2: TestPoint, TestPoint:TestPoint_Pad_2.0x2.0mm, B.Cu at (192.6, 163.2)
- added GND2: TestPoint, TestPoint:TestPoint_Pad_2.0x2.0mm, B.Cu at (252.4, 45.7)
- added GND2: TestPoint, TestPoint:TestPoint_Pad_2.0x2.0mm, B.Cu at (206.9, 45.7)
- added GND2: TestPoint, TestPoint:TestPoint_Pad_2.0x2.0mm, B.Cu at (74.7, 45.7)
- added GND2: TestPoint, TestPoint:TestPoint_Pad_2.0x2.0mm, B.Cu at (118.0, 45.7)
- added GND2: TestPoint, TestPoint:TestPoint_Pad_2.0x2.0mm, B.Cu at (51.2, 163.8)
- added GND2: TestPoint, TestPoint:TestPoint_Pad_2.0x2.0mm, B.Cu at (163.5, 45.7)
- added INTERRUPT_GPIO1: SW_Push, Connector_Wire:SolderWire-0.1sqmm_1x02_P3.6mm_D0.4mm_OD1mm, B.Cu at (97.2, 73.3)
- added INTERRUPT_GPIO1: SW_Push, Connector_Wire:SolderWire-0.1sqmm_1x02_P3.6mm_D0.4mm_OD1mm, B.Cu at (186.1, 73.3)
- added INTERRUPT_GPIO1: SW_Push, Connector_Wire:SolderWire-0.1sqmm_1x02_P3.6mm_D0.4mm_OD1mm, B.Cu at (275.0, 73.3)
- added INTERRUPT_GPIO1: SW_Push, Connector_Wire:SolderWire-0.1sqmm_1x02_P3.6mm_D0.4mm_OD1mm, B.Cu at (229.5, 73.3)
- added INTERRUPT_GPIO1: SW_Push, Connector_Wire:SolderWire-0.1sqmm_1x02_P3.6mm_D0.4mm_OD1mm, B.Cu at (140.6, 73.3)
- added INTERRUPT_GPIO1: SW_Push, Connector_Wire:SolderWire-0.1sqmm_1x02_P3.6mm_D0.4mm_OD1mm, B.Cu at (220.1, 140.6)
- added INTERRUPT_GPIO1: SW_Push, Connector_Wire:SolderWire-0.1sqmm_1x02_P3.6mm_D0.4mm_OD1mm, B.Cu at (78.8, 141.2)
- added R1: 120, Resistor_THT:R_Axial_DIN0204_L3.6mm_D1.6mm_P7.62mm_Horizontal, F.Cu at (263.1, 38.3)
- added R1: 120, Resistor_THT:R_Axial_DIN0204_L3.6mm_D1.6mm_P7.62mm_Horizontal, F.Cu at (85.3, 38.3)
- added R1: 120, Resistor_THT:R_Axial_DIN0204_L3.6mm_D1.6mm_P7.62mm_Horizontal, F.Cu at (185.1, 152.5)
- added R1: 120, Resistor_THT:R_Axial_DIN0204_L3.6mm_D1.6mm_P7.62mm_Horizontal, F.Cu at (128.6, 38.3)
- added R1: 120, Resistor_THT:R_Axial_DIN0204_L3.6mm_D1.6mm_P7.62mm_Horizontal, F.Cu at (43.7, 153.2)
- added R1: 120, Resistor_THT:R_Axial_DIN0204_L3.6mm_D1.6mm_P7.62mm_Horizontal, F.Cu at (217.5, 38.3)
- added R1: 120, Resistor_THT:R_Axial_DIN0204_L3.6mm_D1.6mm_P7.62mm_Horizontal, F.Cu at (174.2, 38.3)
- added R2: 27K, Resistor_THT:R_Axial_DIN0204_L3.6mm_D1.6mm_P7.62mm_Horizontal, F.Cu at (249.4, 38.2)
- added R2: 27K, Resistor_THT:R_Axial_DIN0204_L3.6mm_D1.6mm_P7.62mm_Horizontal, F.Cu at (160.5, 38.2)
- added R2: 27K, Resistor_THT:R_Axial_DIN0204_L3.6mm_D1.6mm_P7.62mm_Horizontal, F.Cu at (43.7, 166.9)
- added R2: 27K, Resistor_THT:R_Axial_DIN0204_L3.6mm_D1.6mm_P7.62mm_Horizontal, F.Cu at (26.1, 38.2)
- added R2: 27K, Resistor_THT:R_Axial_DIN0204_L3.6mm_D1.6mm_P7.62mm_Horizontal, F.Cu at (114.9, 38.2)
- added R2: 27K, Resistor_THT:R_Axial_DIN0204_L3.6mm_D1.6mm_P7.62mm_Horizontal, F.Cu at (185.1, 166.2)
- added R2: 27K, Resistor_THT:R_Axial_DIN0204_L3.6mm_D1.6mm_P7.62mm_Horizontal, F.Cu at (203.8, 38.2)
- added R2: 27K, Resistor_THT:R_Axial_DIN0204_L3.6mm_D1.6mm_P7.62mm_Horizontal, F.Cu at (71.6, 38.2)
- added R3: 100K, Resistor_THT:R_Axial_DIN0204_L3.6mm_D1.6mm_P7.62mm_Horizontal, F.Cu at (43.7, 162.6)
- added R3: 100K, Resistor_THT:R_Axial_DIN0204_L3.6mm_D1.6mm_P7.62mm_Horizontal, F.Cu at (185.1, 161.9)
- added R3: 100K, Resistor_THT:R_Axial_DIN0204_L3.6mm_D1.6mm_P7.62mm_Horizontal, F.Cu at (30.4, 38.2)
- added R3: 100K, Resistor_THT:R_Axial_DIN0204_L3.6mm_D1.6mm_P7.62mm_Horizontal, F.Cu at (119.3, 38.2)
- added R3: 100K, Resistor_THT:R_Axial_DIN0204_L3.6mm_D1.6mm_P7.62mm_Horizontal, F.Cu at (164.8, 38.2)
- added R3: 100K, Resistor_THT:R_Axial_DIN0204_L3.6mm_D1.6mm_P7.62mm_Horizontal, F.Cu at (208.2, 38.2)
- added R3: 100K, Resistor_THT:R_Axial_DIN0204_L3.6mm_D1.6mm_P7.62mm_Horizontal, F.Cu at (253.7, 38.2)
- added R3: 100K, Resistor_THT:R_Axial_DIN0204_L3.6mm_D1.6mm_P7.62mm_Horizontal, F.Cu at (75.9, 38.2)
- added R4: 120, Resistor_THT:R_Axial_DIN0204_L3.6mm_D1.6mm_P7.62mm_Horizontal, F.Cu at (170.0, 38.3)
- added R4: 120, Resistor_THT:R_Axial_DIN0204_L3.6mm_D1.6mm_P7.62mm_Horizontal, F.Cu at (124.5, 38.3)
- added R4: 120, Resistor_THT:R_Axial_DIN0204_L3.6mm_D1.6mm_P7.62mm_Horizontal, F.Cu at (43.7, 157.4)
- added R4: 120, Resistor_THT:R_Axial_DIN0204_L3.6mm_D1.6mm_P7.62mm_Horizontal, F.Cu at (81.1, 38.3)
- added R4: 120, Resistor_THT:R_Axial_DIN0204_L3.6mm_D1.6mm_P7.62mm_Horizontal, F.Cu at (213.4, 38.3)
- added R4: 120, Resistor_THT:R_Axial_DIN0204_L3.6mm_D1.6mm_P7.62mm_Horizontal, F.Cu at (258.9, 38.3)
- added R4: 120, Resistor_THT:R_Axial_DIN0204_L3.6mm_D1.6mm_P7.62mm_Horizontal, F.Cu at (185.1, 156.7)
- added REF**: MountingHole_2.2mm_M2, MountingHole:MountingHole_2.2mm_M2, F.Cu at (157.6, 114.5)
- added REF**: MountingHole_2.2mm_M2, MountingHole:MountingHole_2.2mm_M2, F.Cu at (228.7, 17.7)
- added REF**: MountingHole_2.2mm_M2, MountingHole:MountingHole_2.2mm_M2, F.Cu at (273.9, 114.5)
- added REF**: MountingHole_2.2mm_M2, MountingHole:MountingHole_2.2mm_M2, F.Cu at (96.1, 114.5)
- added REF**: MountingHole_2.2mm_M2, MountingHole:MountingHole_2.2mm_M2, F.Cu at (228.3, 114.5)
- added REF**: MountingHole_2.2mm_M2, MountingHole:MountingHole_2.2mm_M2, F.Cu at (261.4, 141.7)
- added REF**: MountingHole_2.2mm_M2, MountingHole:MountingHole_2.2mm_M2, F.Cu at (139.4, 114.5)
- added REF**: MountingHole_2.2mm_M2, MountingHole:MountingHole_2.2mm_M2, F.Cu at (96.5, 17.7)
- added REF**: MountingHole_2.2mm_M2, MountingHole:MountingHole_2.2mm_M2, F.Cu at (120.0, 169.7)
- added REF**: MountingHole_2.2mm_M2, MountingHole:MountingHole_2.2mm_M2, F.Cu at (201.0, 17.7)
- added REF**: MountingHole_2.2mm_M2, MountingHole:MountingHole_2.2mm_M2, F.Cu at (120.0, 142.4)
- added REF**: MountingHole_2.2mm_M2, MountingHole:MountingHole_2.2mm_M2, F.Cu at (157.6, 17.7)
- added REF**: MountingHole_2.2mm_M2, MountingHole:MountingHole_2.2mm_M2, F.Cu at (246.5, 114.5)
- added REF**: MountingHole_2.2mm_M2, MountingHole:MountingHole_2.2mm_M2, F.Cu at (23.2, 142.0)
- added REF**: MountingHole_2.2mm_M2, MountingHole:MountingHole_2.2mm_M2, F.Cu at (68.8, 17.7)
- added REF**: MountingHole_2.2mm_M2, MountingHole:MountingHole_2.2mm_M2, F.Cu at (23.2, 169.7)
- added REF**: MountingHole_2.2mm_M2, MountingHole:MountingHole_2.2mm_M2, F.Cu at (112.1, 17.7)
- added REF**: MountingHole_2.2mm_M2, MountingHole:MountingHole_2.2mm_M2, F.Cu at (185.0, 114.5)
- added REF**: MountingHole_2.2mm_M2, MountingHole:MountingHole_2.2mm_M2, F.Cu at (139.8, 17.7)
- added REF**: MountingHole_2.2mm_M2, MountingHole:MountingHole_2.2mm_M2, F.Cu at (274.3, 17.7)
- added REF**: MountingHole_2.2mm_M2, MountingHole:MountingHole_2.2mm_M2, F.Cu at (185.4, 17.7)
- added REF**: MountingHole_2.2mm_M2, MountingHole:MountingHole_2.2mm_M2, F.Cu at (68.7, 114.5)
- added REF**: MountingHole_2.2mm_M2, MountingHole:MountingHole_2.2mm_M2, F.Cu at (112.1, 114.5)
- added REF**: MountingHole_2.2mm_M2, MountingHole:MountingHole_2.2mm_M2, F.Cu at (201.0, 114.5)
- added REF**: MountingHole_2.2mm_M2, MountingHole:MountingHole_2.2mm_M2, F.Cu at (164.6, 141.3)
- added REF**: MountingHole_2.2mm_M2, MountingHole:MountingHole_2.2mm_M2, F.Cu at (261.4, 169.1)
- added REF**: MountingHole_2.2mm_M2, MountingHole:MountingHole_2.2mm_M2, F.Cu at (246.5, 17.7)
- added REF**: MountingHole_2.2mm_M2, MountingHole:MountingHole_2.2mm_M2, F.Cu at (164.6, 169.1)
- added SCL1: TestPoint, TestPoint:TestPoint_Pad_2.0x2.0mm, B.Cu at (174.3, 45.7)
- added SCL1: TestPoint, TestPoint:TestPoint_Pad_2.0x2.0mm, B.Cu at (128.8, 45.7)
- added SCL1: TestPoint, TestPoint:TestPoint_Pad_2.0x2.0mm, B.Cu at (51.2, 153.1)
- added SCL1: TestPoint, TestPoint:TestPoint_Pad_2.0x2.0mm, B.Cu at (85.4, 45.7)
- added SCL1: TestPoint, TestPoint:TestPoint_Pad_2.0x2.0mm, B.Cu at (192.6, 152.4)
- added SCL1: TestPoint, TestPoint:TestPoint_Pad_2.0x2.0mm, B.Cu at (263.2, 45.7)
- added SCL1: TestPoint, TestPoint:TestPoint_Pad_2.0x2.0mm, B.Cu at (217.7, 45.7)
- added SDA1: TestPoint, TestPoint:TestPoint_Pad_2.0x2.0mm, B.Cu at (268.3, 45.7)
- added SDA1: TestPoint, TestPoint:TestPoint_Pad_2.0x2.0mm, B.Cu at (179.4, 45.7)
- added SDA1: TestPoint, TestPoint:TestPoint_Pad_2.0x2.0mm, B.Cu at (192.6, 147.3)
- added SDA1: TestPoint, TestPoint:TestPoint_Pad_2.0x2.0mm, B.Cu at (222.7, 45.7)
- added SDA1: TestPoint, TestPoint:TestPoint_Pad_2.0x2.0mm, B.Cu at (90.5, 45.7)
- added SDA1: TestPoint, TestPoint:TestPoint_Pad_2.0x2.0mm, B.Cu at (51.2, 148.0)
- added SDA1: TestPoint, TestPoint:TestPoint_Pad_2.0x2.0mm, B.Cu at (133.8, 45.7)
- added SIGNAL_IN1: TestPoint, TestPoint:TestPoint_Keystone_5015_Micro-Minature, B.Cu at (125.7, 17.8)
- added SIGNAL_IN1: TestPoint, TestPoint:TestPoint_Keystone_5015_Micro-Minature, B.Cu at (23.3, 156.1)
- added SIGNAL_IN1: TestPoint, TestPoint:TestPoint_Keystone_5015_Micro-Minature, B.Cu at (260.1, 17.8)
- added SIGNAL_IN1: TestPoint, TestPoint:TestPoint_Keystone_5015_Micro-Minature, B.Cu at (82.3, 17.8)
- added SIGNAL_IN1: TestPoint, TestPoint:TestPoint_Keystone_5015_Micro-Minature, B.Cu at (171.2, 17.8)
- added SIGNAL_IN1: TestPoint, TestPoint:TestPoint_Keystone_5015_Micro-Minature, B.Cu at (164.7, 155.5)
- added SIGNAL_IN1: TestPoint, TestPoint:TestPoint_Keystone_5015_Micro-Minature, B.Cu at (214.6, 17.8)
- added U1: ESP32_DevKit_V1_DOIT, esp32_devkit_v1_doit:esp32_devkit_v1_doit, F.Cu at (213.8, 85.9)
- added U1: ESP32_DevKit_V1_DOIT, esp32_devkit_v1_doit:esp32_devkit_v1_doit, F.Cu at (259.3, 85.9)
- added U1: ESP32_DevKit_V1_DOIT, esp32_devkit_v1_doit:esp32_devkit_v1_doit, F.Cu at (81.6, 85.9)
- added U1: ESP32_DevKit_V1_DOIT, esp32_devkit_v1_doit:esp32_devkit_v1_doit, F.Cu at (91.4, 156.9)
- added U1: ESP32_DevKit_V1_DOIT, esp32_devkit_v1_doit:esp32_devkit_v1_doit, F.Cu at (124.9, 85.9)
- added U1: ESP32_DevKit_V1_DOIT, esp32_devkit_v1_doit:esp32_devkit_v1_doit, F.Cu at (170.4, 85.9)
- added U1: ESP32_DevKit_V1_DOIT, esp32_devkit_v1_doit:esp32_devkit_v1_doit, F.Cu at (232.8, 156.3)
- added VCC1: TestPoint, TestPoint:TestPoint_Pad_2.0x2.0mm, B.Cu at (123.7, 45.7)
- added VCC1: TestPoint, TestPoint:TestPoint_Pad_2.0x2.0mm, B.Cu at (51.2, 158.1)
- added VCC1: TestPoint, TestPoint:TestPoint_Pad_2.0x2.0mm, B.Cu at (169.2, 45.7)
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- renumbered R2 to R4, SDA1 to SCL1, SCL1 to SDA1
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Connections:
- net Net-(BATTERY1-Pad1) renamed VIN
- U1 pad 7: unconnected-(U1-Pad7) -> Net-(R2-Pad1)
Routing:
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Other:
- board size 254.1 x 158.2 mm -> 256.6 x 157.9 mm
- board text added: "R4k4210 & KremoWy"
